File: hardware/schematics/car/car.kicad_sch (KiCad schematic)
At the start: 6 parts, among them U1 VL53L0CXV0DH1, U2 VL53L0CXV0DH1, U3 VL53L0CXV0DH1, U5 ESP32-C3

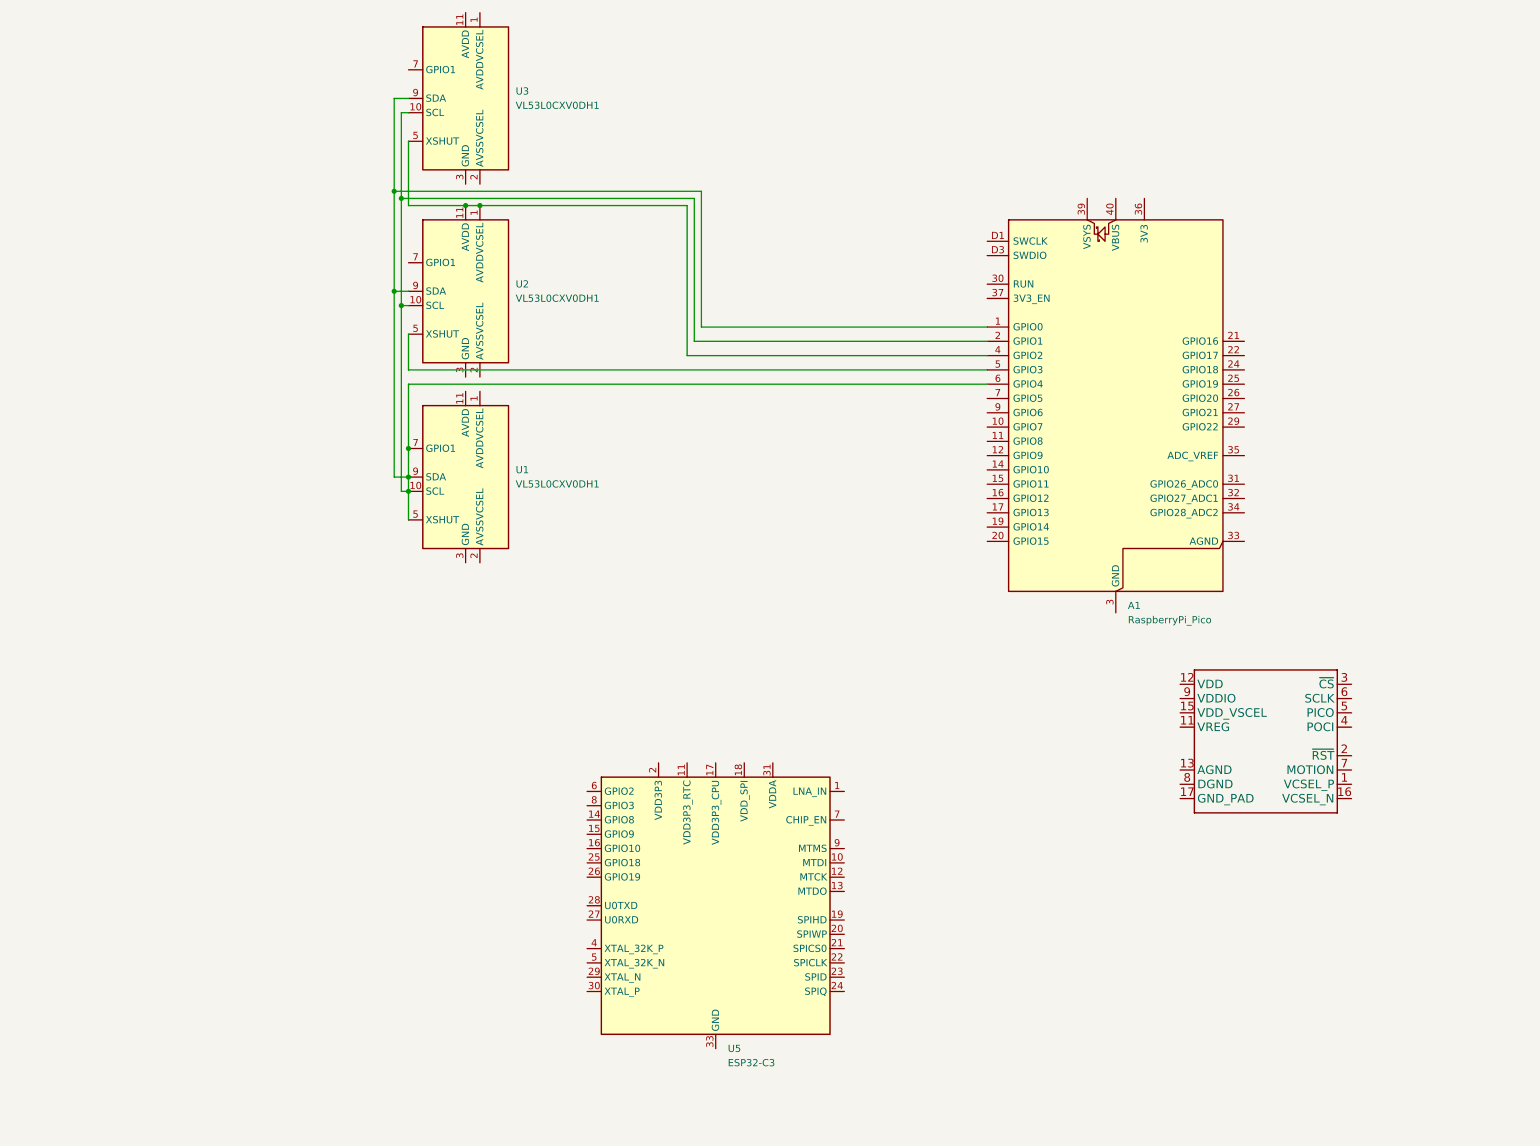
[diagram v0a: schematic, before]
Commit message: [Schematic] Major work. Add: TOFs, Motor, servo, buzzer, ADC(WIP), level shifter. WIP
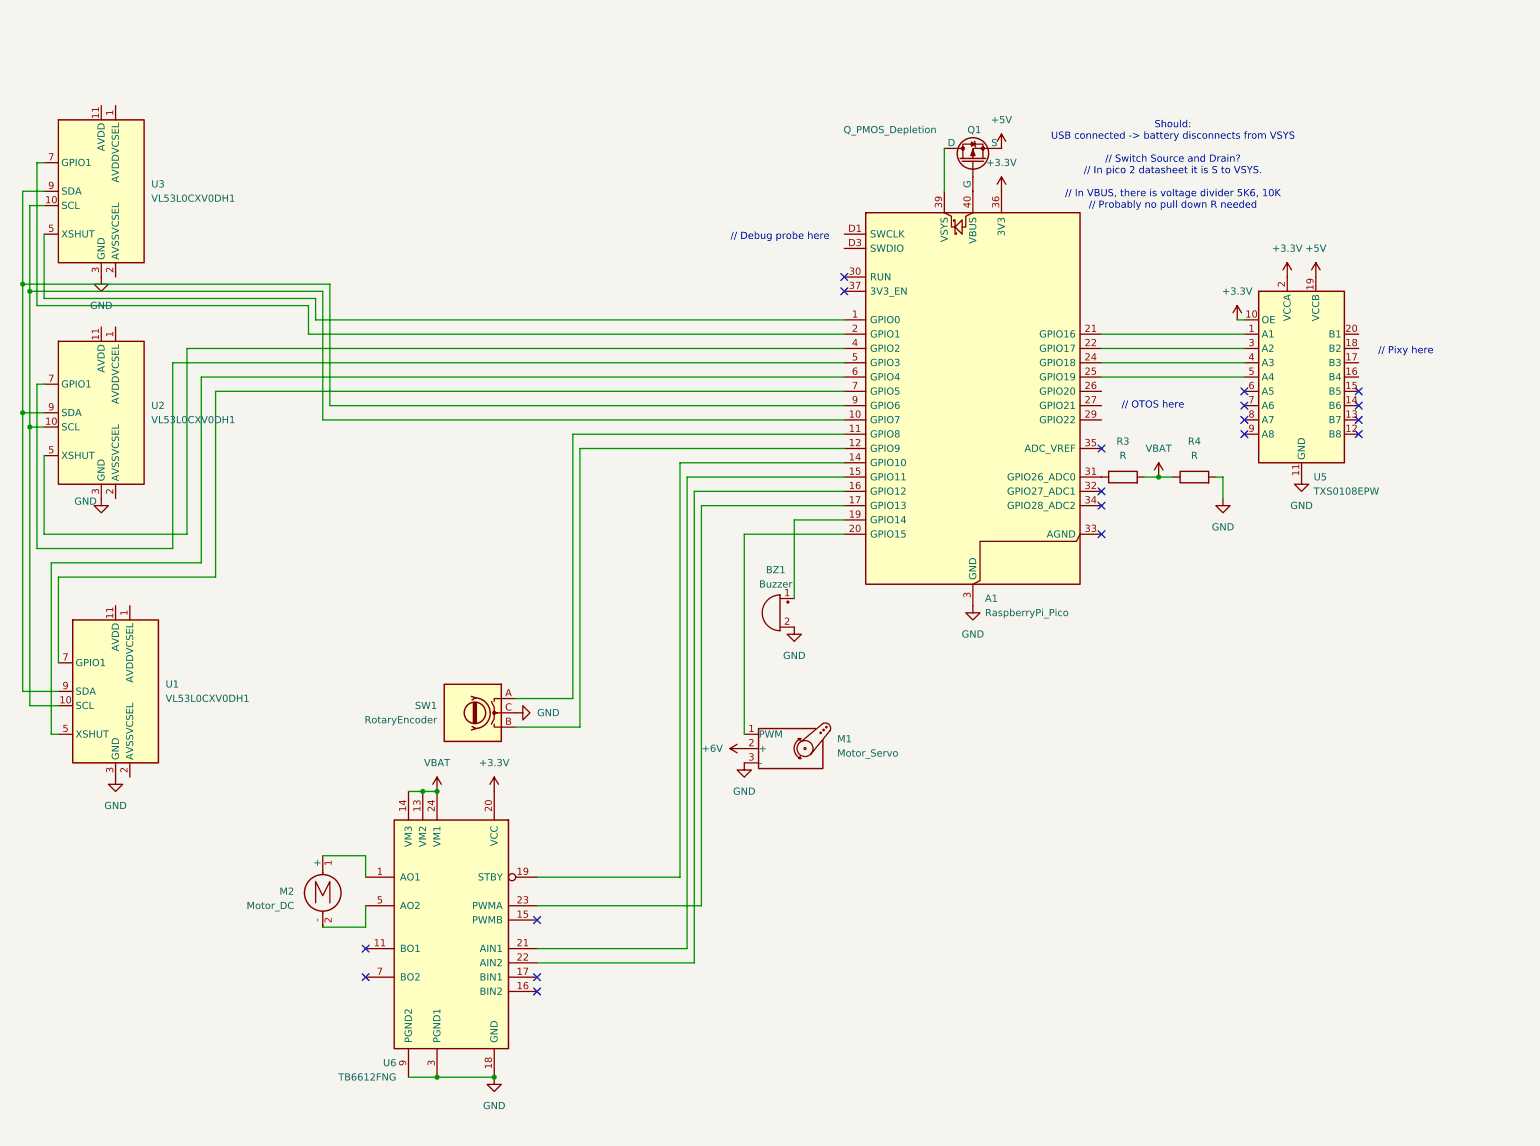
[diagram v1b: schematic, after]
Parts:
- removed U4: (no value), Optical_Tracking_Odometry_Sensor:PAA5160E1-Q, symbol New_Library:PAA5160E1-Q
- removed U5: ESP32-C3, Package_DFN_QFN:QFN-32-1EP_5x5mm_P0.5mm_EP3.7x3.7mm, symbol MCU_Espressif:ESP32-C3
- added BZ1: Buzzer, symbol Device:Buzzer
- added M1: Motor_Servo, Connector_PinHeader_2.54mm:PinHeader_1x03_P2.54mm_Vertical, symbol Motor:Motor_Servo
- added M2: Motor_DC, symbol Motor:Motor_DC
- added Q1: Q_PMOS_Depletion, symbol Device:Q_PMOS_Depletion
- added R3, R4: R, symbol Device:R
- added SW1: RotaryEncoder, symbol Device:RotaryEncoder
- added U5: TXS0108EPW, Package_SO:TSSOP-20_4.4x6.5mm_P0.65mm, symbol Logic_LevelTranslator:TXS0108EPW
- added U6: TB6612FNG, Package_SO:SSOP-24_5.3x8.2mm_P0.65mm, symbol Driver_Motor:TB6612FNG
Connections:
- net GND: now reaches U2.12 (GND), U2.3 (GND), U2.4 (GND), U2.6 (GND)
- net GND: now also A1.13 (GND), A1.18 (GND), A1.23 (GND), A1.28 (GND), A1.3 (GND), A1.38 (GND), A1.8 (GND), A1.D2 (GND), U1.12 (GND), U1.3 (GND), U1.4 (GND), U1.6 (GND), U3.12 (GND), U3.3 (GND), U3.4 (GND), U3.6 (GND), BZ1.2 (-), M1.3 (-), R4.2, SW1.C, U5.11 (GND), U6.10 (PGND2), U6.18 (GND), U6.3 (PGND1), U6.4 (PGND1), U6.9 (PGND2)
- net at U2.5 (XSHUT): now also A1.4 (GPIO2); no longer A1.5 (GPIO3)
- net at U2.7 (GPIO1): now also A1.5 (GPIO3)
- net at U3.7 (GPIO1): now also A1.2 (GPIO1)
- net at A1.10 (GPIO7): now also U1.10 (SCL), U2.10 (SCL), U3.10 (SCL)
- net at A1.11 (GPIO8): now also SW1.A
- net at A1.12 (GPIO9): now also SW1.B
- net at A1.14 (GPIO10): now also U6.19 (STBY)
- net at A1.15 (GPIO11): now also U6.21 (AIN1)
- net at A1.16 (GPIO12): now also U6.22 (AIN2)
- net at A1.17 (GPIO13): now also U6.23 (PWMA)
- net at A1.19 (GPIO14): now also BZ1.1 (+)
- net at A1.20 (GPIO15): now also M1.1 (PWM)
- net at A1.21 (GPIO16): now also U5.1 (A1)
- net at A1.22 (GPIO17): now also U5.3 (A2)
- net at A1.24 (GPIO18): now also U5.4 (A3)
- net at A1.25 (GPIO19): now also U5.5 (A4)
- net at A1.31 (GPIO26_ADC0): now also R3.1
- net +3.3V: now reaches A1.36 (3V3)
- net +3.3V: now also U5.10 (OE), U5.2 (VCCA), U6.20 (VCC)
- net at A1.39 (VSYS): now also Q1.D
- net at A1.40 (VBUS): now also Q1.G
- net at A1.7 (GPIO5): now also U1.7 (GPIO1)
- net at A1.9 (GPIO6): now also U1.9 (SDA), U2.9 (SDA), U3.9 (SDA)
- new net: M2.1 (+), U6.1 (AO1), U6.2 (AO1)
- new net: U6.11 (BO1), U6.12 (BO1)
- new net: M2.2 (-), U6.5 (AO2), U6.6 (AO2)
- new net: U6.7 (BO2), U6.8 (BO2)
- new net: A1.1 (GPIO0), U3.5 (XSHUT)
- new net: A1.6 (GPIO4), U1.5 (XSHUT)
- new net +5V: Q1.S, U5.19 (VCCB)
- new net +6V: M1.2 (+)
- new net VBAT: R3.2, R4.1, U6.13 (VM2), U6.14 (VM3), U6.24 (VM1)
- now unconnected: U2.1 (AVDDVCSEL), U2.11 (AVDD)
- no-connect marks 0 -> 19
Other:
- note added: "// Debug probe here"
- note added: "// OTOS here"
- note added: "// Pixy here"
- note added: "Should: USB connected -> battery disconnects from VSYS // Switch Source and Drain? // In pico 2 datasheet it is S to VSYS. // In VBUS, there is voltage divider 5K6, 10K // Probably no pull down R needed"
- company: (none) -> XLNC APEX
- moved on the sheet: A1, U1, U2, U3

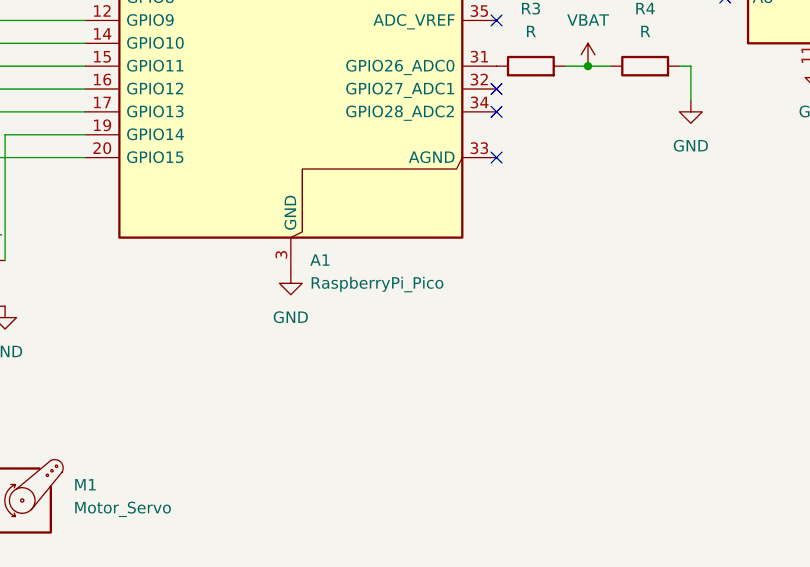
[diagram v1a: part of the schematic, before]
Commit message: [Schematic] Minor: Change datasheet and name to pico 2
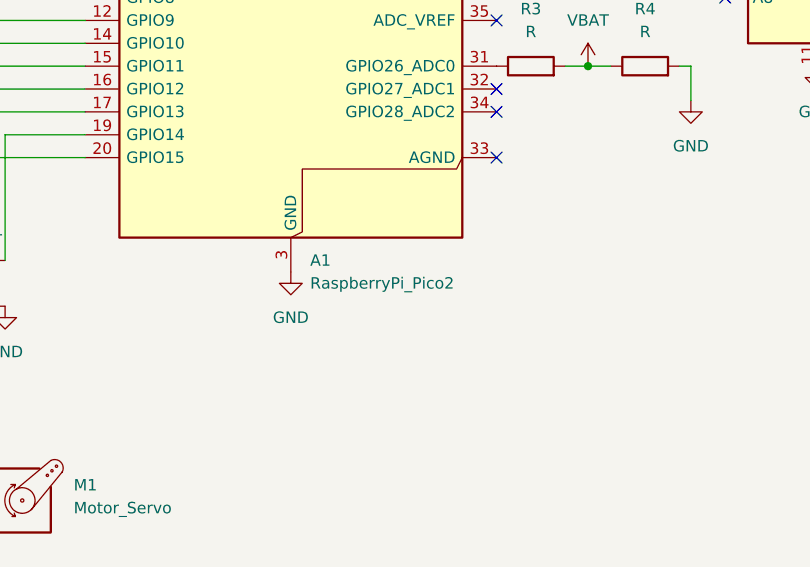
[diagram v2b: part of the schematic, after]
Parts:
- A1: value RaspberryPi_Pico -> RaspberryPi_Pico2
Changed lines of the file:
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@@
 			)
 		)
-		(property "Value" "RaspberryPi_Pico"
+		(property "Value" "RaspberryPi_Pico2"
 			(at 187.5633 104.14 0)
 			(show_name no)
@@
 			)
 		)
-		(property "Datasheet" "https://datasheets.raspberrypi.com/pico/pico-datasheet.pdf"
+		(property "Datasheet" "https://pip.raspberrypi.com/documents/RP-008299-DS"
 			(at 185.42 116.84 0)
 			(hide yes)

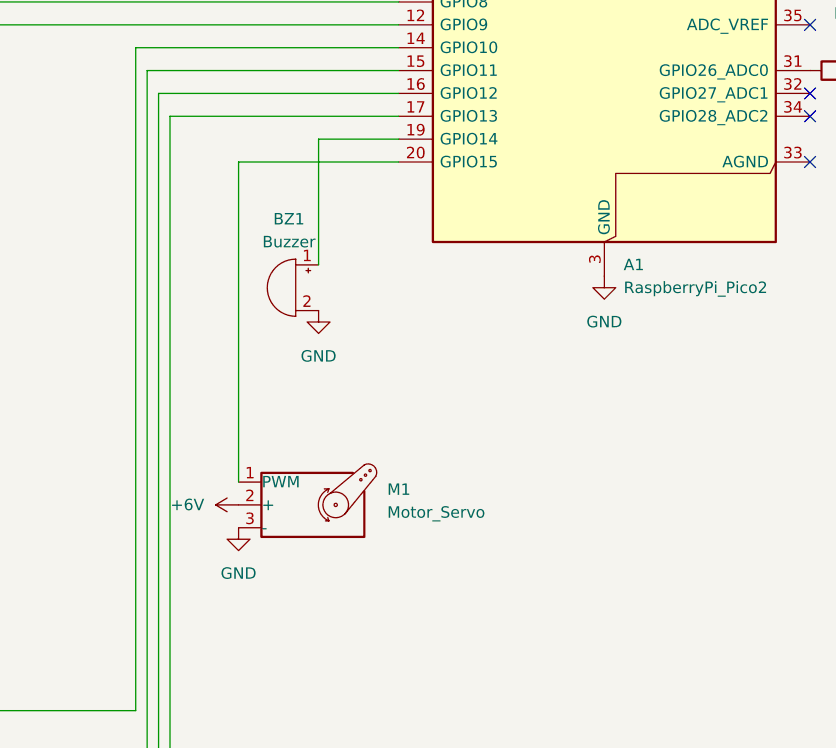
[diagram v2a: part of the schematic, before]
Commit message: [Schematic] Servo: add schottky diode on power 1N5824
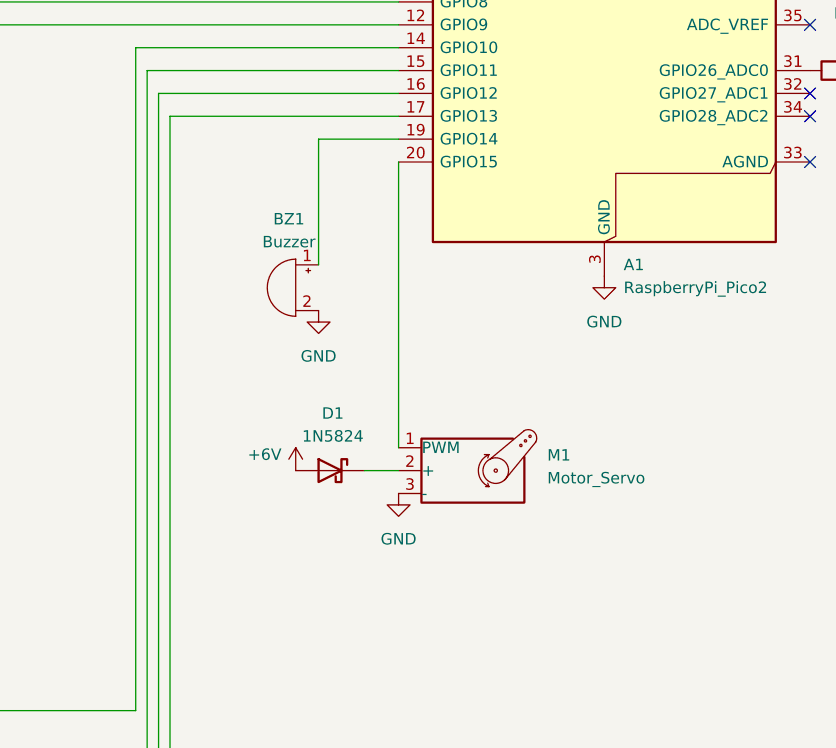
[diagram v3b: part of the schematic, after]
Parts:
- added D1: 1N5824, Diode_THT:D_DO-15_P15.24mm_Horizontal, symbol Device:D_Schottky
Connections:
- net +6V: now also D1.2 (A); no longer M1.2 (+)
- new net: D1.1 (K), M1.2 (+)
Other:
- moved on the sheet: M1
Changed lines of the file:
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@@
 	(wire
 		(pts
+			(xy 158.75 124.46) (xy 162.56 124.46)
+		)
+		(stroke
+			(width 0)
+			(type default)
+		)
+	)
+	(wire
+		(pts
 			(xy 19.05 49.53) (xy 67.31 49.53)
 		)
@@
 	(wire
 		(pts
-			(xy 144.78 90.17) (xy 162.56 90.17)
-		)
-		(stroke
-			(width 0)
-			(type default)
-		)
-	)
-	(wire
-		(pts
 			(xy 16.51 45.72) (xy 16.51 29.21)
 		)
@@
 	(wire
 		(pts
-			(xy 135.89 166.37) (xy 135.89 82.55)
+			(xy 162.56 90.17) (xy 162.56 121.92)
 		)
 		(stroke
@@
 	(wire
 		(pts
-			(xy 144.78 125.73) (xy 144.78 90.17)
+			(xy 135.89 166.37) (xy 135.89 82.55)
 		)
 		(stroke
@@
 	(symbol
 		(lib_id "power:+6V")
-		(at 144.78 128.27 90)
+		(at 151.13 124.46 0)
 		(unit 1)
 		(body_style 1)
@@
 		(in_pos_files yes)
 		(dnp no)
-		(fields_autoplaced yes)
 		(property "Reference" "#PWR09"
-			(at 148.59 128.27 0)
+			(at 151.13 128.27 0)
 			(hide yes)
 			(show_name no)
@@
 		)
 		(property "Value" "+6V"
-			(at 140.97 128.2699 90)
+			(at 145.796 122.682 0)
 			(show_name no)
 			(do_not_autoplace no)
@@
 		)
 		(property "Footprint" ""
-			(at 144.78 128.27 0)
+			(at 151.13 124.46 0)
 			(hide yes)
 			(show_name no)
@@
 		)
 		(property "Datasheet" ""
-			(at 144.78 128.27 0)
+			(at 151.13 124.46 0)
 			(hide yes)
 			(show_name no)
@@
 		)
 		(property "Description" "Power symbol creates a global label with name \"+6V\""
-			(at 144.78 128.27 0)
+			(at 151.13 124.46 0)
 			(hide yes)
 			(show_name no)
@@
 	(symbol
 		(lib_id "Motor:Motor_Servo")
-		(at 152.4 128.27 0)
+		(at 170.18 124.46 0)
 		(unit 1)
 		(body_style 1)
@@
 		(fields_autoplaced yes)
 		(property "Reference" "M1"
-			(at 161.29 126.5668 0)
+			(at 179.07 122.7568 0)
 			(show_name no)
 			(do_not_autoplace no)
@@
 		)
 		(property "Value" "Motor_Servo"
-			(at 161.29 129.1068 0)
+			(at 179.07 125.2968 0)
 			(show_name no)
 			(do_not_autoplace no)
@@
 		)
 		(property "Footprint" "Connector_PinHeader_2.54mm:PinHeader_1x03_P2.54mm_Vertical"
-			(at 152.4 133.096 0)
+			(at 170.18 129.286 0)
 			(hide yes)
 			(show_name no)
@@
 		)
 		(property "Datasheet" "http://forums.parallax.com/uploads/attachments/46831/74481.png"
-			(at 152.4 133.096 0)
+			(at 170.18 129.286 0)
 			(hide yes)
 			(show_name no)
@@
 		)
 		(property "Description" "Servo Motor (Futaba, HiTec, JR connector)"
-			(at 152.4 128.27 0)
+			(at 170.18 124.46 0)
 			(hide yes)
 			(show_name no)
@@
 	(symbol
 		(lib_id "power:GND")
-		(at 144.78 130.81 0)
+		(at 162.56 127 0)
 		(unit 1)
 		(body_style 1)
@@
 		(fields_autoplaced yes)
 		(property "Reference" "#PWR07"
-			(at 144.78 137.16 0)
+			(at 162.56 133.35 0)
 			(hide yes)
 			(show_name no)
@@
 		)
 		(property "Value" "GND"
-			(at 144.78 135.89 0)
+			(at 162.56 132.08 0)
 			(show_name no)
 			(do_not_autoplace no)
@@
 		)
 		(property "Footprint" ""
-			(at 144.78 130.81 0)
+			(at 162.56 127 0)
 			(hide yes)
 			(show_name no)
@@
 		)
 		(property "Datasheet" ""
-			(at 144.78 130.81 0)
+			(at 162.56 127 0)
 			(hide yes)
 			(show_name no)
@@
 		)
 		(property "Description" "Power symbol creates a global label with name \"GND\" , ground"
-			(at 144.78 130.81 0)
+			(at 162.56 127 0)
 			(hide yes)
 			(show_name no)
@@
 					(unit 1)
 				)
+			)
+		)
+	)
+	(symbol
+		(lib_id "Device:D_Schottky")
+		(at 154.94 124.46 0)
+		(mirror y)
+		(unit 1)
+		(body_style 1)
+		(exclude_from_sim no)
+		(in_bom yes)
+		(on_board yes)
+		(in_pos_files yes)
+		(dnp no)
+		(fields_autoplaced yes)
+		(property "Reference" "D1"
+			(at 155.2575 118.11 0)
+			(show_name no)
+			(do_not_autoplace no)
+			(effects
+				(font
+					(size 1.27 1.27)
+				)
+			)
+		)
+		(property "Value" "1N5824"
+			(at 155.2575 120.65 0)
+			(show_name no)
+			(do_not_autoplace no)
+			(effects
+				(font
+					(size 1.27 1.27)
+				)
+			)
+		)
+		(property "Footprint" "Diode_THT:D_DO-15_P15.24mm_Horizontal"
+			(at 154.94 124.46 0)
+			(hide yes)
+			(show_name no)
+			(do_not_autoplace no)
+			(effects
+				(font
+					(size 1.27 1.27)
+				)
+			)
+		)
+		(property "Datasheet" ""
+			(at 154.94 124.46 0)
+			(hide yes)
+			(show_name no)
+			(do_not_autoplace no)
+			(effects
+				(font
+					(size 1.27 1.27)
+				)
+			)
+		)
+		(property "Description" "Schottky diode"
+			(at 154.94 124.46 0)
+			(hide yes)
+			(show_name no)
+			(do_not_autoplace no)
+			(effects
+				(font
+					(size 1.27 1.27)
+				)
+			)
+		)
+		(pin "2"
+		)
+		(pin "1"
+		)
+		(instances
+			(project "car"
+				(path "/5e1ba60a-5dff-4ce7-a8b0-cf19f27fe16e"
+					(reference "D1")
+					(unit 1)
+				)
